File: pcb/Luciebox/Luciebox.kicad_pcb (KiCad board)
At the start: 2 copper layers, 68.6 x 53.3 mm, 20 parts, among them J1 Screw_Terminal_01x07, J2 Screw_Terminal_01x07, J3 Screw_Terminal_01x07, P1 Power, P2 Analog, P3 Digital, P4 Digital, P5 CONN_01X01, P6 CONN_01X01, P7 CONN_01X01, P8 CONN_01X01, Q1 BC558, U1 CA56-12SRWA, U2 ULN2003A, U3 ATmega328-PU

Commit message: pcb progress dedicated R-2R ladder'
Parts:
- added BZ1: Buzzer, Luciebox:buzzer, F.Cu at (134.4, -57.8)
- added C1: 100nF, Luciebox:0805, F.Cu at (125.0, -58.7)
- added C2: 20pF, Luciebox:0805, F.Cu at (125.0, -55.8)
- added C3: 20pF, Luciebox:0805, F.Cu at (125.0, -52.9)
- added J4: Screw_Terminal_01x07, Luciebox:Terminal_7x1_100mil, F.Cu at (118.5, -62.3)
- added R10: 10K, Luciebox:1206, F.Cu at (119.2, -58.5)
- added R11: 10K, Luciebox:1206, F.Cu at (146.4, -66.8)
- added R12: 10K, Luciebox:1206, F.Cu at (112.6, -55.2)
- added R13: 10K, Luciebox:1206, F.Cu at (119.2, -51.8)
- added R14: 10K, Luciebox:1206, F.Cu at (119.2, -48.5)
- added R15: 10K, Luciebox:1206, F.Cu at (125.9, -49.5)
- added R16: 10K, Luciebox:1206, F.Cu at (132.5, -49.5)
- added R17: 10K, Luciebox:1206, F.Cu at (144.2, -59.3)
- added R18: 10K, Luciebox:1206, F.Cu at (139.2, -49.5)
- added R19: 100, Luciebox:1206, F.Cu at (144.2, -55.9)
- added R20: R_Small, Luciebox:1206, F.Cu at (108.5, -18.4)
- added R21: R_Small, Luciebox:1206, F.Cu at (105.9, -18.4)
- added R22: R_Small, Luciebox:1206, F.Cu at (103.4, -18.4)
- added R23: R_Small, Luciebox:1206, F.Cu at (100.8, -18.4)
- added R24: R_Small, Luciebox:1206, F.Cu at (98.3, -19.2)
- added R25: R_Small, Luciebox:1206, F.Cu at (95.8, -18.4)
- added R26: R_Small, Luciebox:1206, F.Cu at (93.2, -18.9)
- added R27: R_Small, Luciebox:1206, F.Cu at (90.7, -19.2)
- added R28: DAC_R-2R, Luciebox:SIP-10, F.Cu at (99.6, -8.26)
- added R29: DAC_R-2R, Luciebox:SIP-10, F.Cu at (174.5, -92.1)
- added R30: DAC_R-2R, Luciebox:SIP-10, F.Cu at (159.3, -1.91)
- added R44: R_Small, Luciebox:1206, F.Cu at (183.4, -104.2)
- added R45: R_Small, Luciebox:1206, F.Cu at (180.8, -103.5)
- added R46: R_Small, Luciebox:1206, F.Cu at (178.3, -103.5)
- added R47: R_Small, Luciebox:1206, F.Cu at (175.8, -103.5)
- added R48: R_Small, Luciebox:1206, F.Cu at (173.2, -103.5)
- added R49: R_Small, Luciebox:1206, F.Cu at (170.7, -104.2)
- added R50: R_Small, Luciebox:1206, F.Cu at (168.1, -103.5)
- added R51: R_Small, Luciebox:1206, F.Cu at (165.6, -104.2)
- added R6: 1M, Luciebox:1206, F.Cu at (119.2, -55.2)
- added R68: R_Small, Luciebox:1206, F.Cu at (168.1, -13.3)
- added R69: R_Small, Luciebox:1206, F.Cu at (165.6, -13.3)
- added R7: 10K, Luciebox:1206, F.Cu at (112.6, -58.5)
- added R70: R_Small, Luciebox:1206, F.Cu at (163.1, -12.8)
- added R71: R_Small, Luciebox:1206, F.Cu at (160.5, -12.8)
- added R72: R_Small, Luciebox:1206, F.Cu at (158.0, -12.8)
- added R73: R_Small, Luciebox:1206, F.Cu at (155.4, -13.3)
- added R74: R_Small, Luciebox:1206, F.Cu at (152.9, -12.8)
- added R75: R_Small, Luciebox:1206, F.Cu at (150.4, -13.3)
- added R8: 10K, Luciebox:1206, F.Cu at (144.2, -62.6)
- added R9: 10K, Luciebox:1206, F.Cu at (112.6, -49.5)
- added RV1: R_POT, Luciebox:0805, F.Cu at (143.3, -52.8)
- added T1: terminal_13x1, Luciebox:Terminal_13x1_100mil, F.Cu at (126.1, -66.4)
- added T2: terminal_8x1, Luciebox:Terminal_8x1_100mil, F.Cu at (99.6, -12.1)
- added T3: terminal_8x1, Luciebox:Terminal_8x1_100mil, F.Cu at (174.5, -98.4)
- added T4: terminal_8x1, Luciebox:Terminal_8x1_100mil, F.Cu at (159.3, -6.99)
- added Y1: 16MHz, Luciebox:buzzer, F.Cu at (150.6, -47.6)
- J1, J2, J3: footprint Luciebox:Term_Block_1x7_P5.08mm -> Luciebox:Terminal_7x1_100mil
- P1: value Power -> CONN_01X01; footprint Socket_Arduino_Uno:Socket_Strip_Arduino_1x08 -> Socket_Arduino_Uno:Arduino_1pin
- P2: value Analog -> CONN_01X01; footprint Socket_Arduino_Uno:Socket_Strip_Arduino_1x06 -> Socket_Arduino_Uno:Arduino_1pin
- P3: value Digital -> CONN_01X01; footprint Socket_Arduino_Uno:Socket_Strip_Arduino_1x10 -> Socket_Arduino_Uno:Arduino_1pin
- P4: value Digital -> CONN_01X01; footprint Socket_Arduino_Uno:Socket_Strip_Arduino_1x08 -> Socket_Arduino_Uno:Arduino_1pin
- P5: value CONN_01X01 -> Digital; footprint Socket_Arduino_Uno:Arduino_1pin -> Socket_Arduino_Uno:Socket_Strip_Arduino_1x10
- P6: value CONN_01X01 -> Power; footprint Socket_Arduino_Uno:Arduino_1pin -> Socket_Arduino_Uno:Socket_Strip_Arduino_1x08
- P7: value CONN_01X01 -> Digital; footprint Socket_Arduino_Uno:Arduino_1pin -> Socket_Arduino_Uno:Socket_Strip_Arduino_1x08
- P8: value CONN_01X01 -> Analog; footprint Socket_Arduino_Uno:Arduino_1pin -> Socket_Arduino_Uno:Socket_Strip_Arduino_1x06
- R1: renamed from R5; value R_Small -> 100
- R2: renamed from R1; value R_Small -> 100
- R3: renamed from R2; value R_Small -> 100
- R4: renamed from R3; value R_Small -> 100
- R5: renamed from R4; value R_Small -> 100
- moved U3 108.0 mm to (205.0, 3.17)
- moved P5 48.5 mm to (129.8, 75.6)
- moved P6 38.4 mm to (138.9, 123.8)
- moved P8 36.4 mm to (161.8, 123.8)
- moved P7 30.5 mm to (156.7, 75.6)
- moved P4 25.4 mm to (177.0, 90.8)
- moved J2 20.7 mm to (192.3, 131.4)
- moved P2 16.1 mm to (177.0, 118.7)
- moved P1 14.0 mm to (125.0, 123.8)
- moved P3 3.56 mm to (126.2, 75.6)
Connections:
- P2 pad 1: /A0 -> Net-(P2-Pad1)
- P3 pad 1: /A5(SCL) -> Net-(P3-Pad1)
- P4 pad 1: /7 -> Net-(P4-Pad1)
- P5 pad 1: Net-(P5-Pad1) -> /A5(SCL)
- P7 pad 1: Net-(P7-Pad1) -> /7
- P8 pad 1: Net-(P8-Pad1) -> /A0
- U3 pad 11: Net-(U3-Pad11) -> /5(PWM)
- U3 pad 12: Net-(U3-Pad12) -> /6(PWM)
- U3 pad 13: Net-(U3-Pad13) -> /7
- U3 pad 14: Net-(U3-Pad14) -> /8
- U3 pad 15: Net-(U3-Pad15) -> /9(PWM)
- U3 pad 16: Net-(U3-Pad16) -> /10(PWM-SS)
- U3 pad 17: Net-(U3-Pad17) -> /11(PWM-MOSI)
- U3 pad 18: Net-(U3-Pad18) -> /12(MISO)
- U3 pad 19: Net-(U3-Pad19) -> /13(SCK)
- U3 pad 2: Net-(U3-Pad2) -> /0(Rx)
- U3 pad 20: Net-(U3-Pad20) -> VCC
- U3 pad 21: Net-(U3-Pad21) -> VCC
- U3 pad 22: Net-(U3-Pad22) -> GND
- U3 pad 23: Net-(U3-Pad23) -> /A0
- U3 pad 24: Net-(U3-Pad24) -> /A1
- U3 pad 25: Net-(U3-Pad25) -> /A2
- U3 pad 26: Net-(U3-Pad26) -> /A3
- U3 pad 27: Net-(U3-Pad27) -> /A4(SDA)
- U3 pad 28: Net-(U3-Pad28) -> /A5(SCL)
- U3 pad 3: Net-(U3-Pad3) -> /1(Tx)
- U3 pad 4: Net-(U3-Pad4) -> /2
- U3 pad 5: Net-(U3-Pad5) -> /3(PWM)
- U3 pad 6: Net-(U3-Pad6) -> /4
- U3 pad 7: Net-(U3-Pad7) -> VCC
- U3 pad 8: Net-(U3-Pad22) -> GND

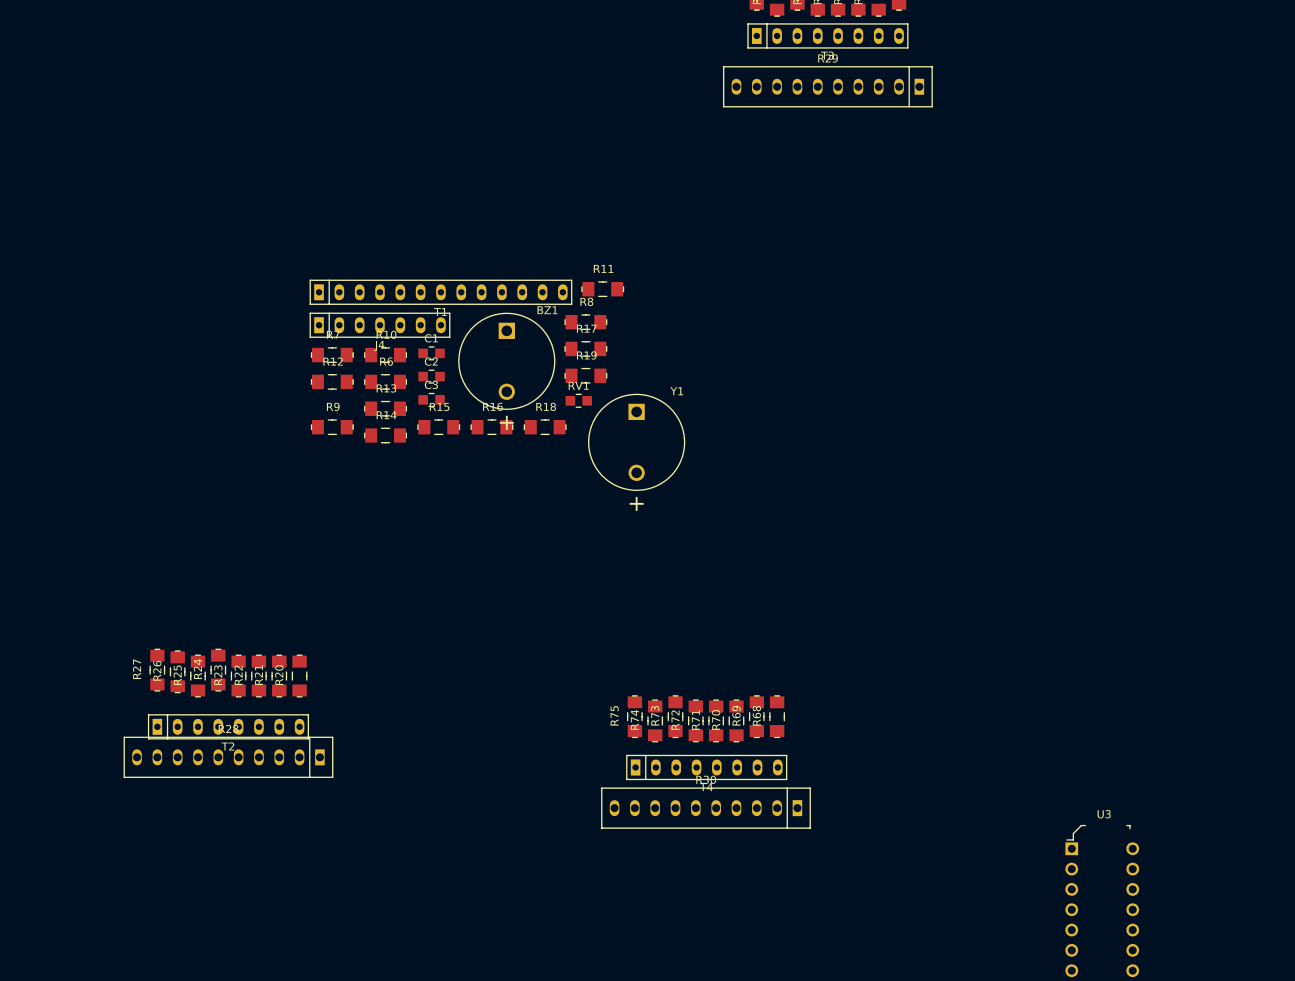
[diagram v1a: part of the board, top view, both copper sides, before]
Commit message: pcb selector resistors
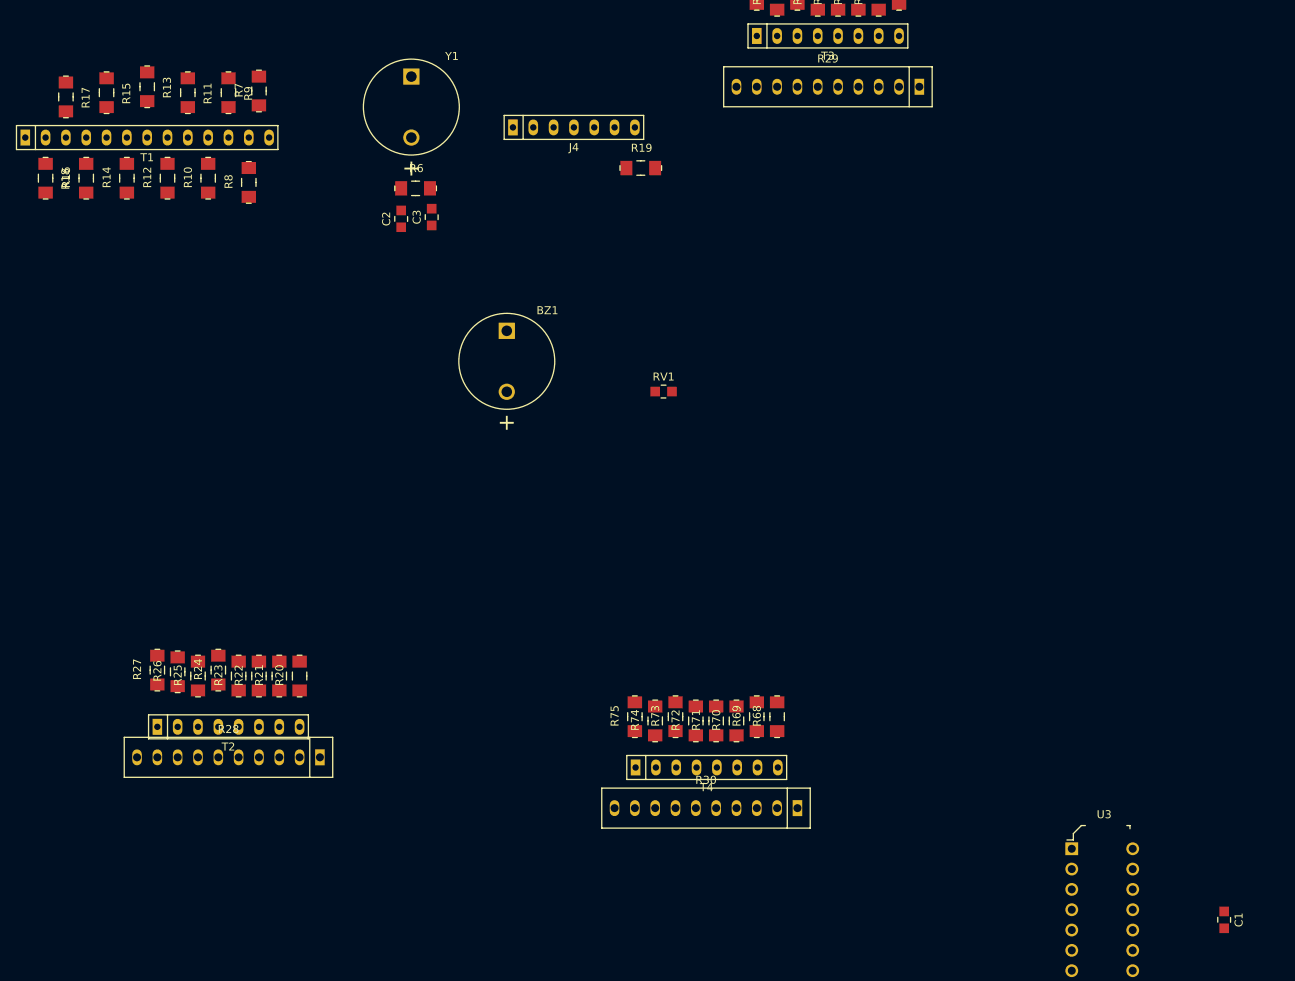
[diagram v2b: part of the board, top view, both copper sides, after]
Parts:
- moved C1 121.8 mm to (224.0, 12.1), turned to 270 degrees
- moved R17 72.2 mm to (79.2, -90.8), turned to 270 degrees
- moved R18 69.8 mm to (76.7, -80.6), turned to 270 degrees
- moved R16 59.5 mm to (81.8, -80.6), turned to 90 degrees
- moved R15 58.9 mm to (84.3, -91.3), turned to 270 degrees
- moved R11 57.4 mm to (94.5, -91.3), turned to 270 degrees
- moved Y1 50.5 mm to (122.4, -89.5)
- moved R13 50.1 mm to (89.4, -92.1), turned to 270 degrees
- moved R8 45.6 mm to (102.1, -80.1), turned to 90 degrees
- moved R14 45.6 mm to (86.9, -80.6), turned to 90 degrees
- moved R9 43.8 mm to (99.6, -91.3), turned to 270 degrees
- moved T1 41.5 mm to (89.4, -85.7)
- moved J4 34.6 mm to (142.7, -87.0)
- moved R7 34.3 mm to (103.4, -91.5), turned to 90 degrees
- moved R12 32.8 mm to (91.9, -80.6), turned to 90 degrees
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
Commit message: working on pcb of luciebox
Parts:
- added T2: terminal_8x1, Luciebox:Terminal_8x1_100mil, F.Cu at (99.6, -27.3)
- added T3: terminal_8x1, Luciebox:Terminal_8x1_100mil, F.Cu at (99.6, -23.5)
- added T5: terminal_8x1, Luciebox:Terminal_8x1_100mil, F.Cu at (174.5, -109.9)
- added T6: terminal_8x1, Luciebox:Terminal_8x1_100mil, F.Cu at (174.5, -113.7)
- added T8: terminal_8x1, Luciebox:Terminal_8x1_100mil, F.Cu at (163.3, 52.3)
- added T9: terminal_8x1, Luciebox:Terminal_8x1_100mil, F.Cu at (163.3, 55.5)
- moved P2 254.4 mm to (-75.0, 84.3), turned to 180 degrees
- moved P4 253.0 mm to (-75.0, 112.2), turned to 180 degrees
- moved P8 226.0 mm to (-59.8, 79.2), turned to 180 degrees
- moved P7 217.7 mm to (-54.7, 127.4), turned to 180 degrees
- moved R10 207.9 mm to (246.0, 64.4)
- moved R11 207.9 mm to (243.5, 53.7)
- moved R12 207.9 mm to (240.9, 64.4)
- moved R13 207.9 mm to (238.4, 52.9)
- moved R14 207.9 mm to (235.9, 64.4)
- moved R15 207.9 mm to (233.3, 53.7)
- moved R16 207.9 mm to (230.8, 64.4)
- moved R17 207.9 mm to (228.2, 54.2)
- moved R18 207.9 mm to (225.7, 64.4)
- moved R7 207.9 mm to (252.4, 53.5)
- moved R8 207.9 mm to (251.1, 64.9)
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- renumbered R44 to R29, R45 to R30, R46 to R31, R47 to R32, R48 to R33, R49 to R34, R50 to R35, R51 to R36, R29 to R37, R68 to R38, R69 to R39, R70 to R40, R71 to R41, R72 to R42, R73 to R43, R74 to R44, R75 to R45, R30 to R46, T4 to T10, T2 to T4, T3 to T7
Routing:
- net VCC: track 0.00 -> 17.8 mm
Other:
- board size 68.6 x 53.3 mm -> 555.6 x 134.8 mm

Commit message: pcb organize components
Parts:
- moved R37 241.9 mm to (121.6, 144.0)
- moved R29 241.9 mm to (130.5, 131.8)
- moved R30 241.9 mm to (128.0, 132.6)
- moved R31 241.9 mm to (125.4, 132.6)
- moved R32 241.9 mm to (122.9, 132.6)
- moved R33 241.9 mm to (120.4, 132.6)
- moved R34 241.9 mm to (117.8, 131.8)
- moved R35 241.9 mm to (115.3, 132.6)
- moved R36 241.9 mm to (112.7, 131.8)
- moved T5 241.9 mm to (121.6, 126.2)
- moved T6 241.9 mm to (121.6, 122.4)
- moved T7 241.9 mm to (121.6, 137.7)
- moved Y1 200.3 mm to (88.9, 107.9), turned to 90 degrees
- moved R6 188.3 mm to (99.0, 107.4), turned to 90 degrees
- moved C2 185.6 mm to (102.8, 109.2), turned to 180 degrees
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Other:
- board size 555.6 x 134.8 mm -> 100 x 100 mm

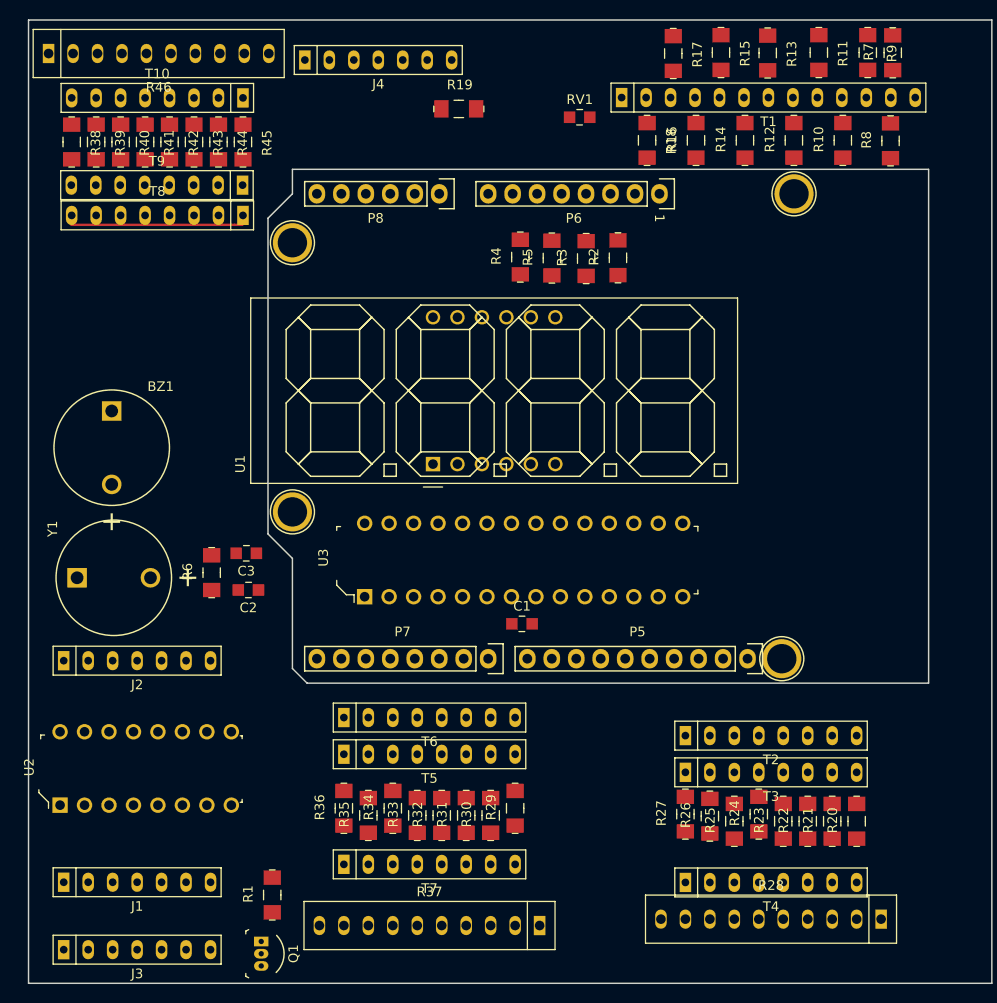
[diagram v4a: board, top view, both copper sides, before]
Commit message: all components have footprint. All fitting on board.
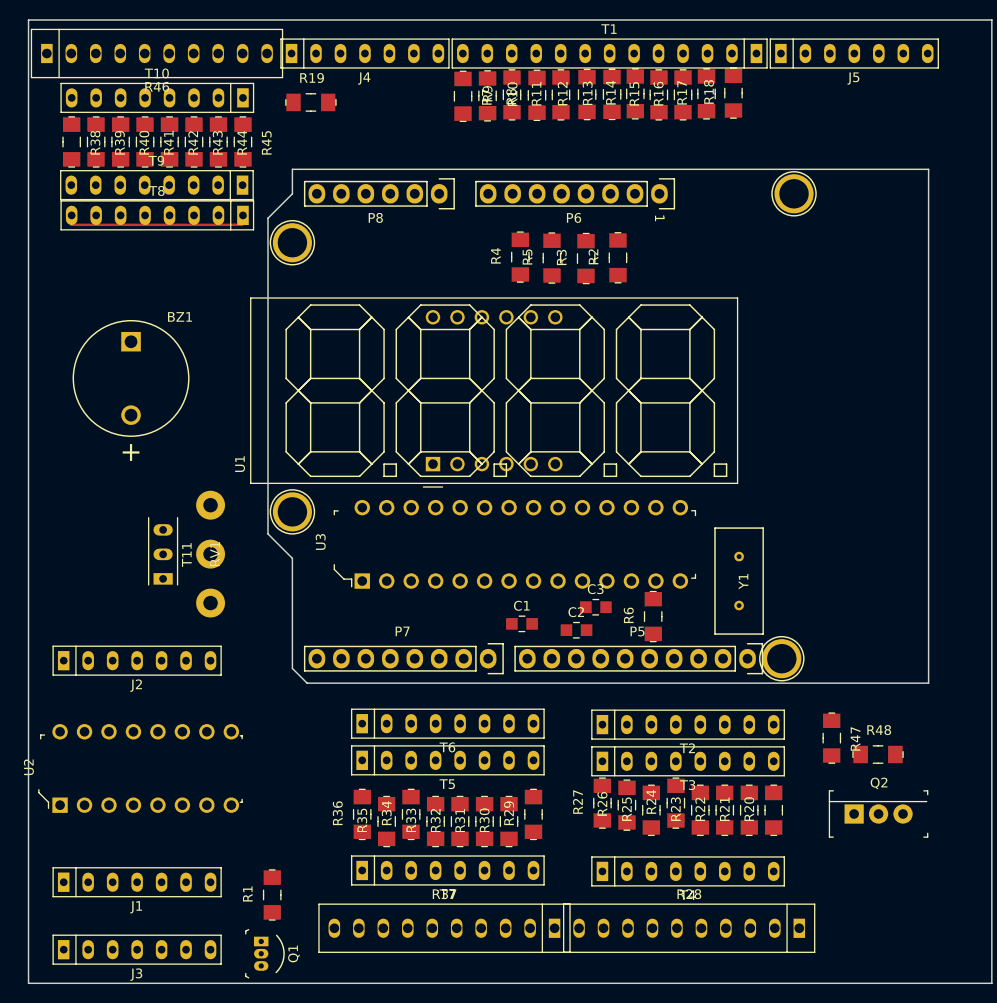
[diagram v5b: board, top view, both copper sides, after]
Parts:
- added J5: Screw_Terminal_01x07, Luciebox:Terminal_7x1_100mil, F.Cu at (165.7, 53.5)
- added Q2: N-Channel_Mosfet, Luciebox:TO-220-3, F.Cu at (165.7, 132.4)
- added R47: 100K, Luciebox:1206, F.Cu at (163.4, 124.5)
- added R48: 100K, Luciebox:1206, F.Cu at (168.2, 126.3)
- added T11: terminal_3x1, Luciebox:Terminal_3x1_100mil, F.Cu at (94.0, 105.5)
- RV1: footprint Luciebox:0805 -> Luciebox:BIG_POTENTIO
- Y1: footprint Luciebox:buzzer -> Luciebox:CRYSTAL
- moved Y1 64.9 mm to (153.8, 108.2)
- moved RV1 59.4 mm to (98.9, 105.4), turned to 90 degrees
- moved R6 46.1 mm to (144.8, 111.9)
- moved R7 44.8 mm to (125.1, 57.9), turned to 270 degrees
- moved R8 42.1 mm to (127.7, 57.9), turned to 270 degrees
- moved R9 37.2 mm to (130.2, 57.8), turned to 90 degrees
- moved C3 36.7 mm to (138.9, 111.0), turned to 0 degrees
- moved C2 34.3 mm to (136.9, 113.3), turned to 0 degrees
- moved R10 32.1 mm to (132.8, 57.8)
- moved R11 27.1 mm to (135.3, 57.8), turned to 90 degrees
- moved R12 22.0 mm to (138.0, 57.7)
- moved T1 17.1 mm to (140.3, 53.5), turned to 180 degrees
- moved R13 16.7 mm to (140.6, 57.7), turned to 90 degrees
- moved R19 15.4 mm to (109.3, 58.6)
- moved R14 12.4 mm to (143.0, 57.7)
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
